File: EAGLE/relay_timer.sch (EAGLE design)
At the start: 25 parts, among them IC1 7805, K1 G2R2, Q1 32.768KHz, T1 BC547, U1 PIC16F886-I/SP, U2 DS1306+

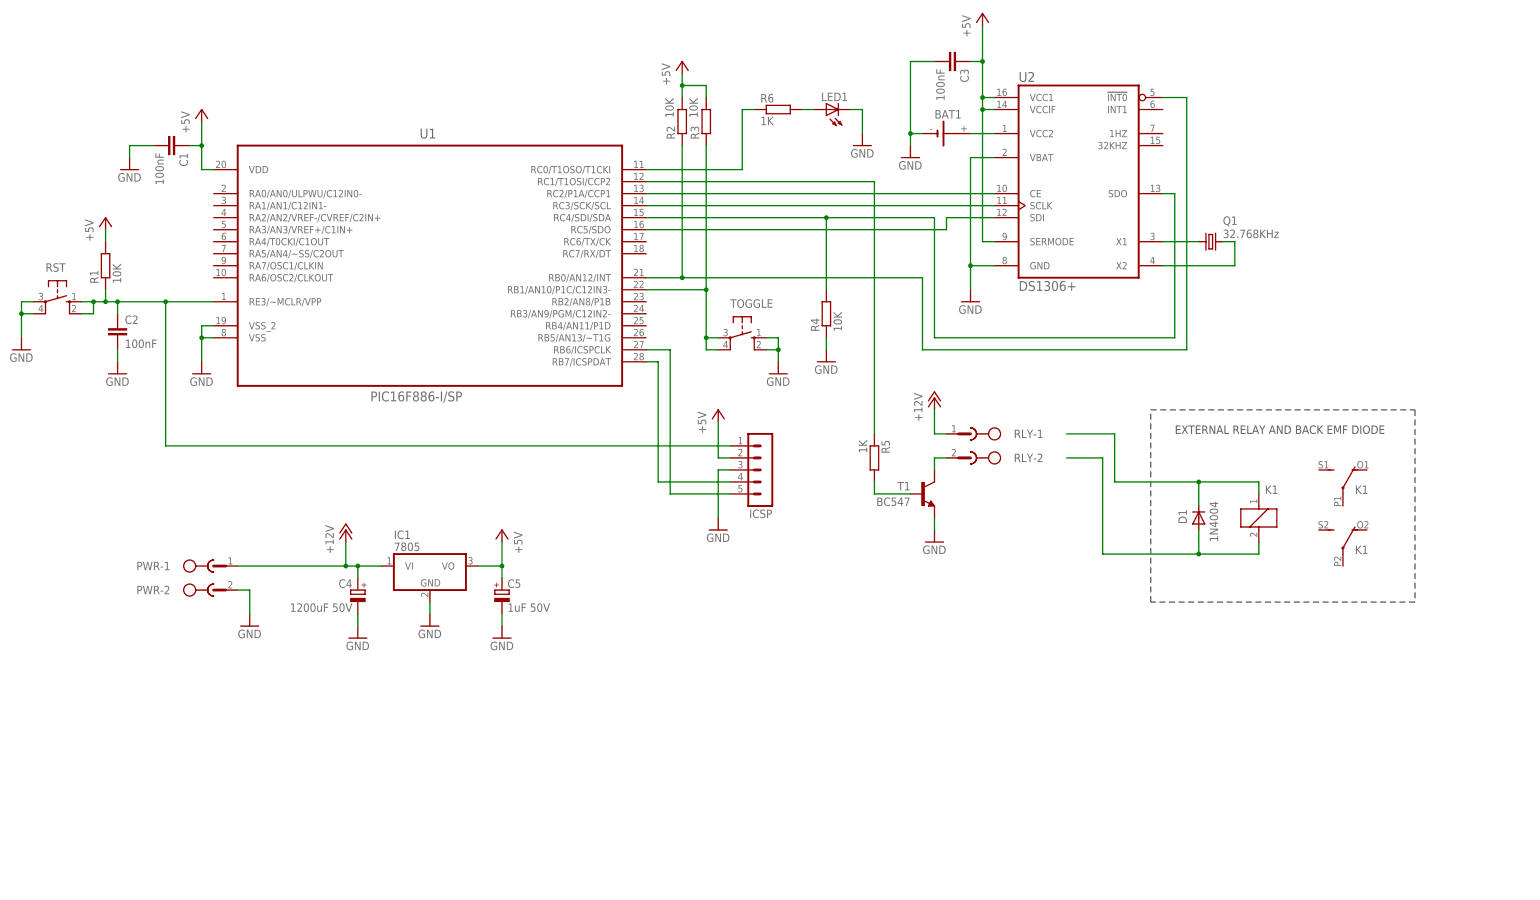
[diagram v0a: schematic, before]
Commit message: Major overhaul of project
Hardware:

* Introduced a second relay which can be used for sequencing the connection of PV and battery to a charger

Software:

* Re-wrote software to be "task based" with some rudimentary concepts
* Support for sequencing the two relays with approx 1 second delay between
* Added ability to extend charging hours during the mid year period
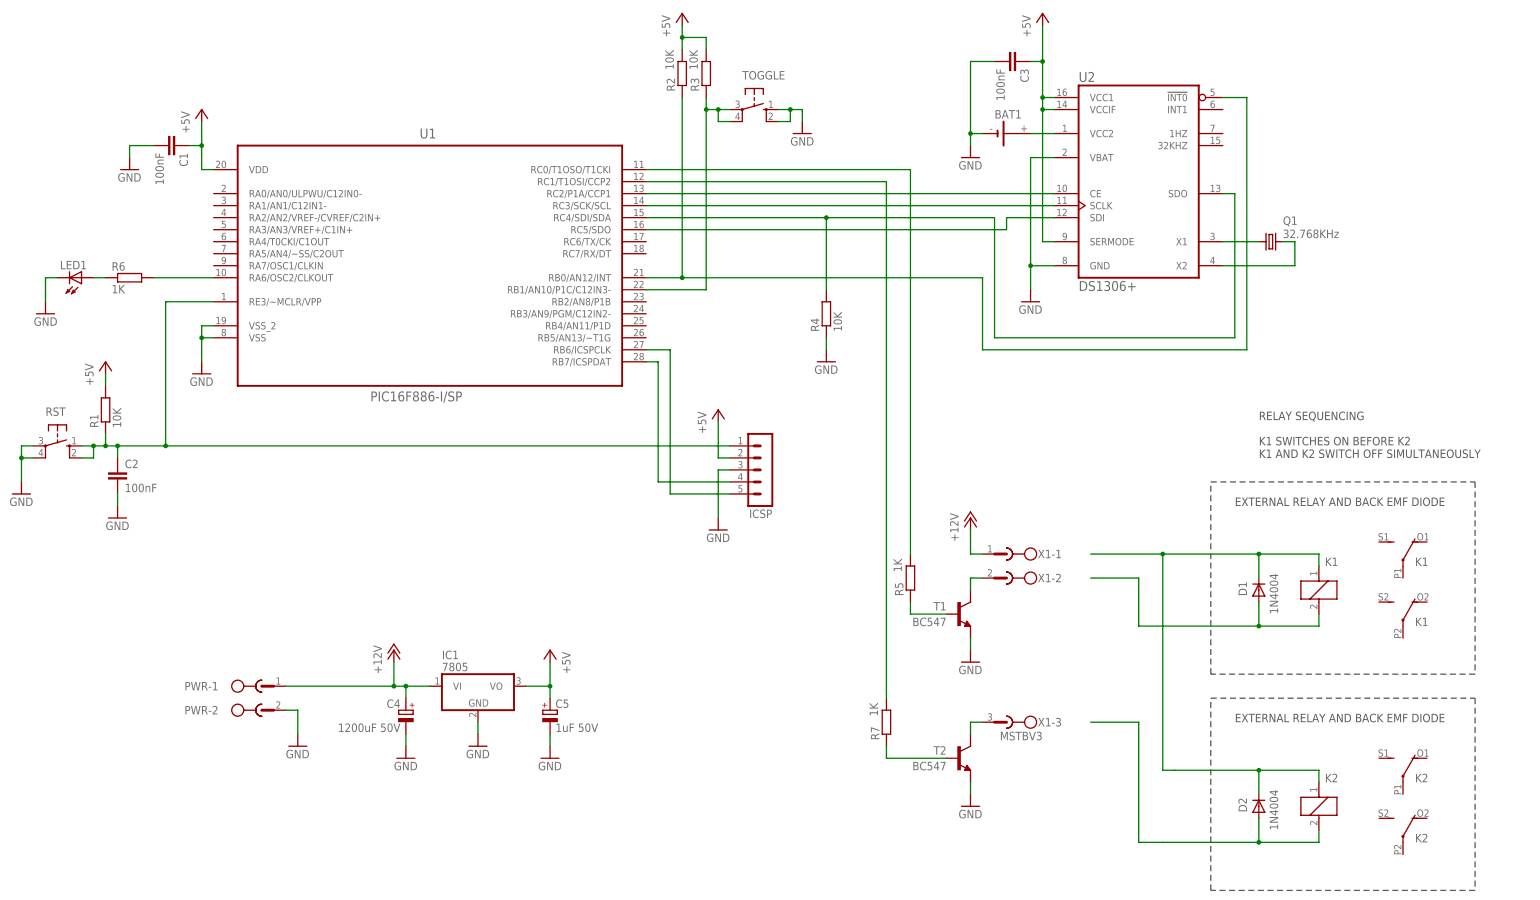
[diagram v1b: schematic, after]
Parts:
- removed RLY: MSTBV2, con-phoenix-508:MSTBV2
- added D2: 1N4004, diode:1N4004
- added K2: G2R2, relay:G2R2
- added R7: 1K, rcl:R-EU_0207/10
- added T2: BC547, transistor:BC547A-NPN-TO92-CBE
- added X1: MSTBV3, con-phoenix-508:MSTBV3
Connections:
- removed net N$18 (its old number): D1.C, K11.1
- new net N$20: R7.1, T2.B
- new net N$21: T2.C, X1-3.1
- new net N$22: D1.C, D2.C, K11.1, K21.1
- new net N$23: D2.A, K21.2
- new net N$9: LED1.A, R6.1
- net +12V: now also X1-1.1; no longer RLY-1.1
- net GND: now also T2.E
- net N$10: now also R5.2, U1.RC0/T1OSO/T1CKI; no longer R5.1, U1.RC1/T1OSI/CCP2
- net N$11: now also R5.1; no longer R5.2
- net N$14: now also X1-2.1; no longer RLY-2.1
- net N$15: now also U1.RA6/OSC2/CLKOUT; no longer LED1.A
- net N$16: now also R7.2, U1.RC1/T1OSI/CCP2; no longer R6.1, U1.RC0/T1OSO/T1CKI
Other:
- note added: "RELAY SEQUENCING K1 SWITCHES ON BEFORE K2 K1 AND K2 SWITCH OFF SIMULTANEOUSLY"
- moved on the sheet: BAT1, C2, C3, C4, C5, D1, IC1, K1, LED1, PWR-1, PWR-2, Q1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
